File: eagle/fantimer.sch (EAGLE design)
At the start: 20 parts, among them IC1 PIC10F220, K1 PB2032-ND, Q1 2N7000-G, U1 IRM-01-5, X1 732-10957-ND

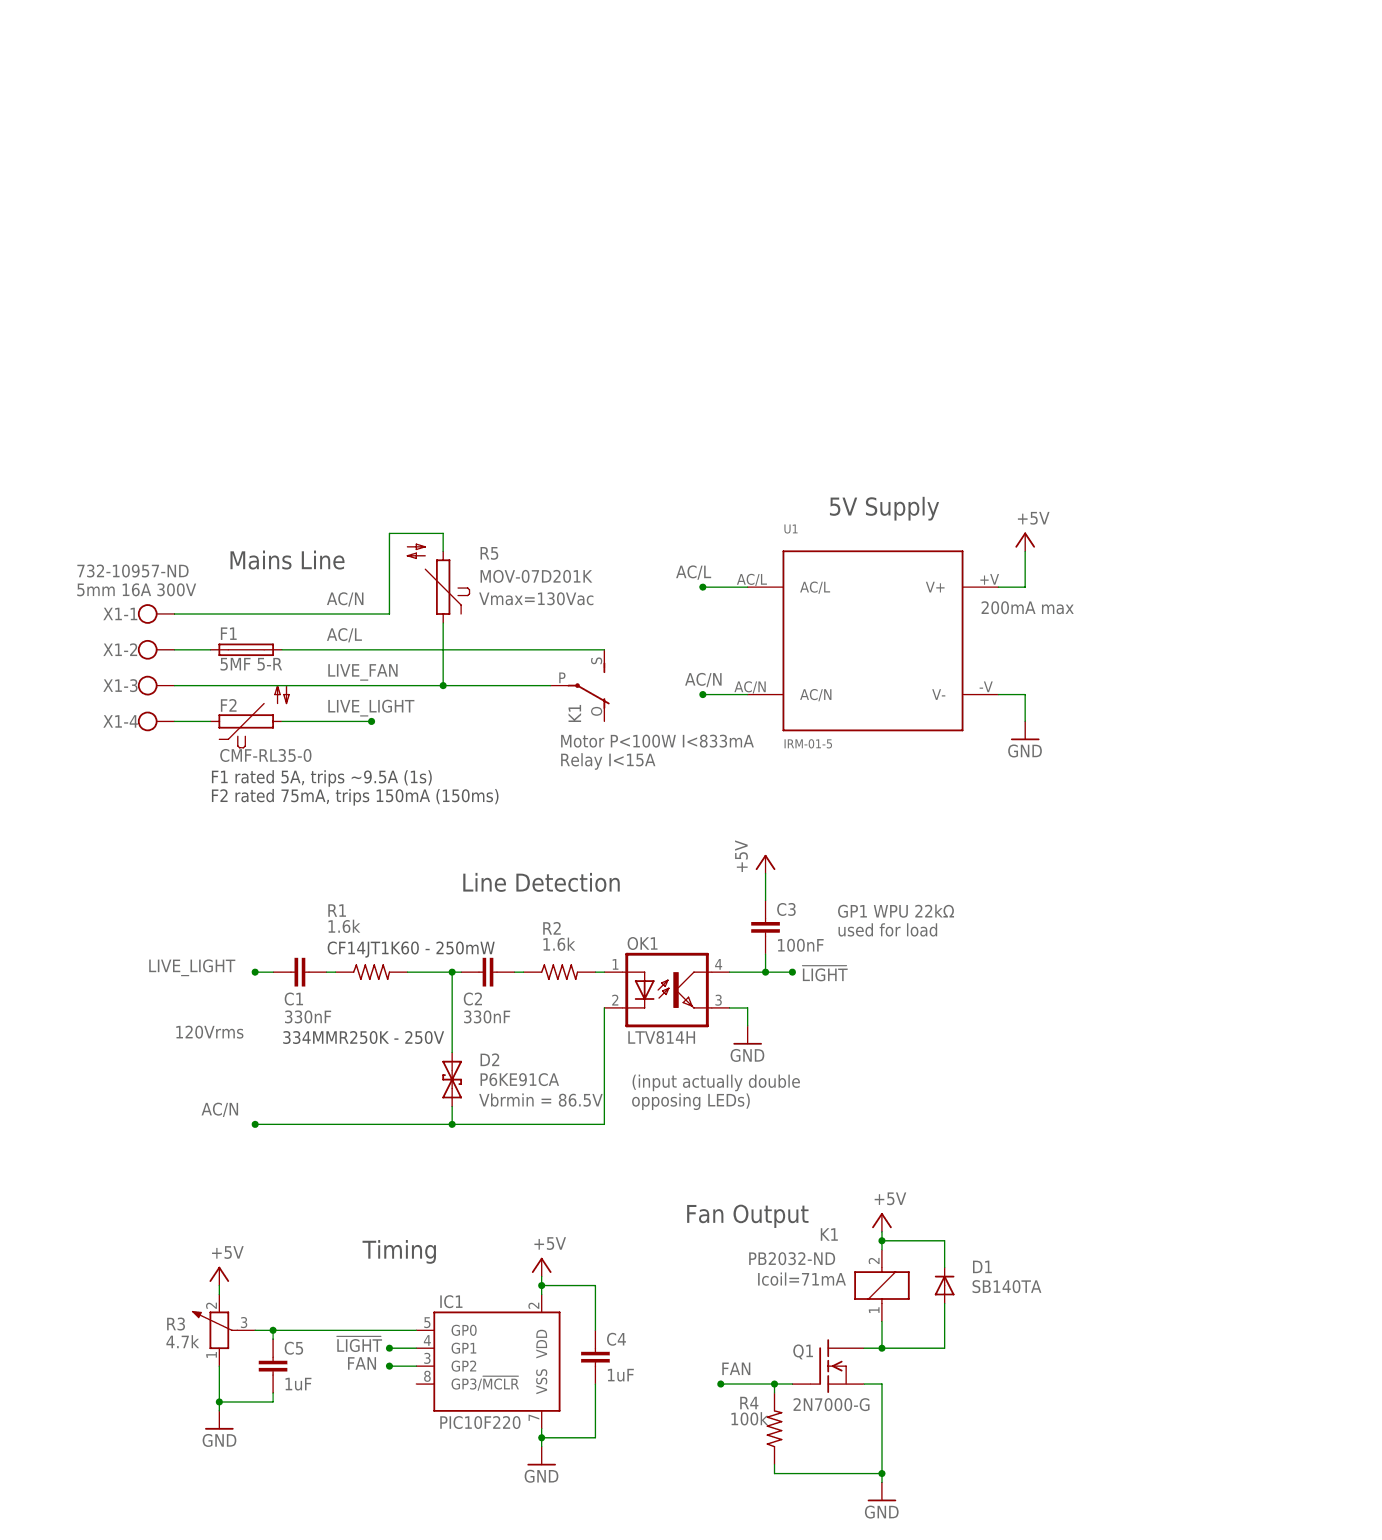
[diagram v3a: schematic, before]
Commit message: Split apart terminal pins to represent circuit logically. Swap terminal 3+4 for better routing. Drop intro text from asm. General report edits.
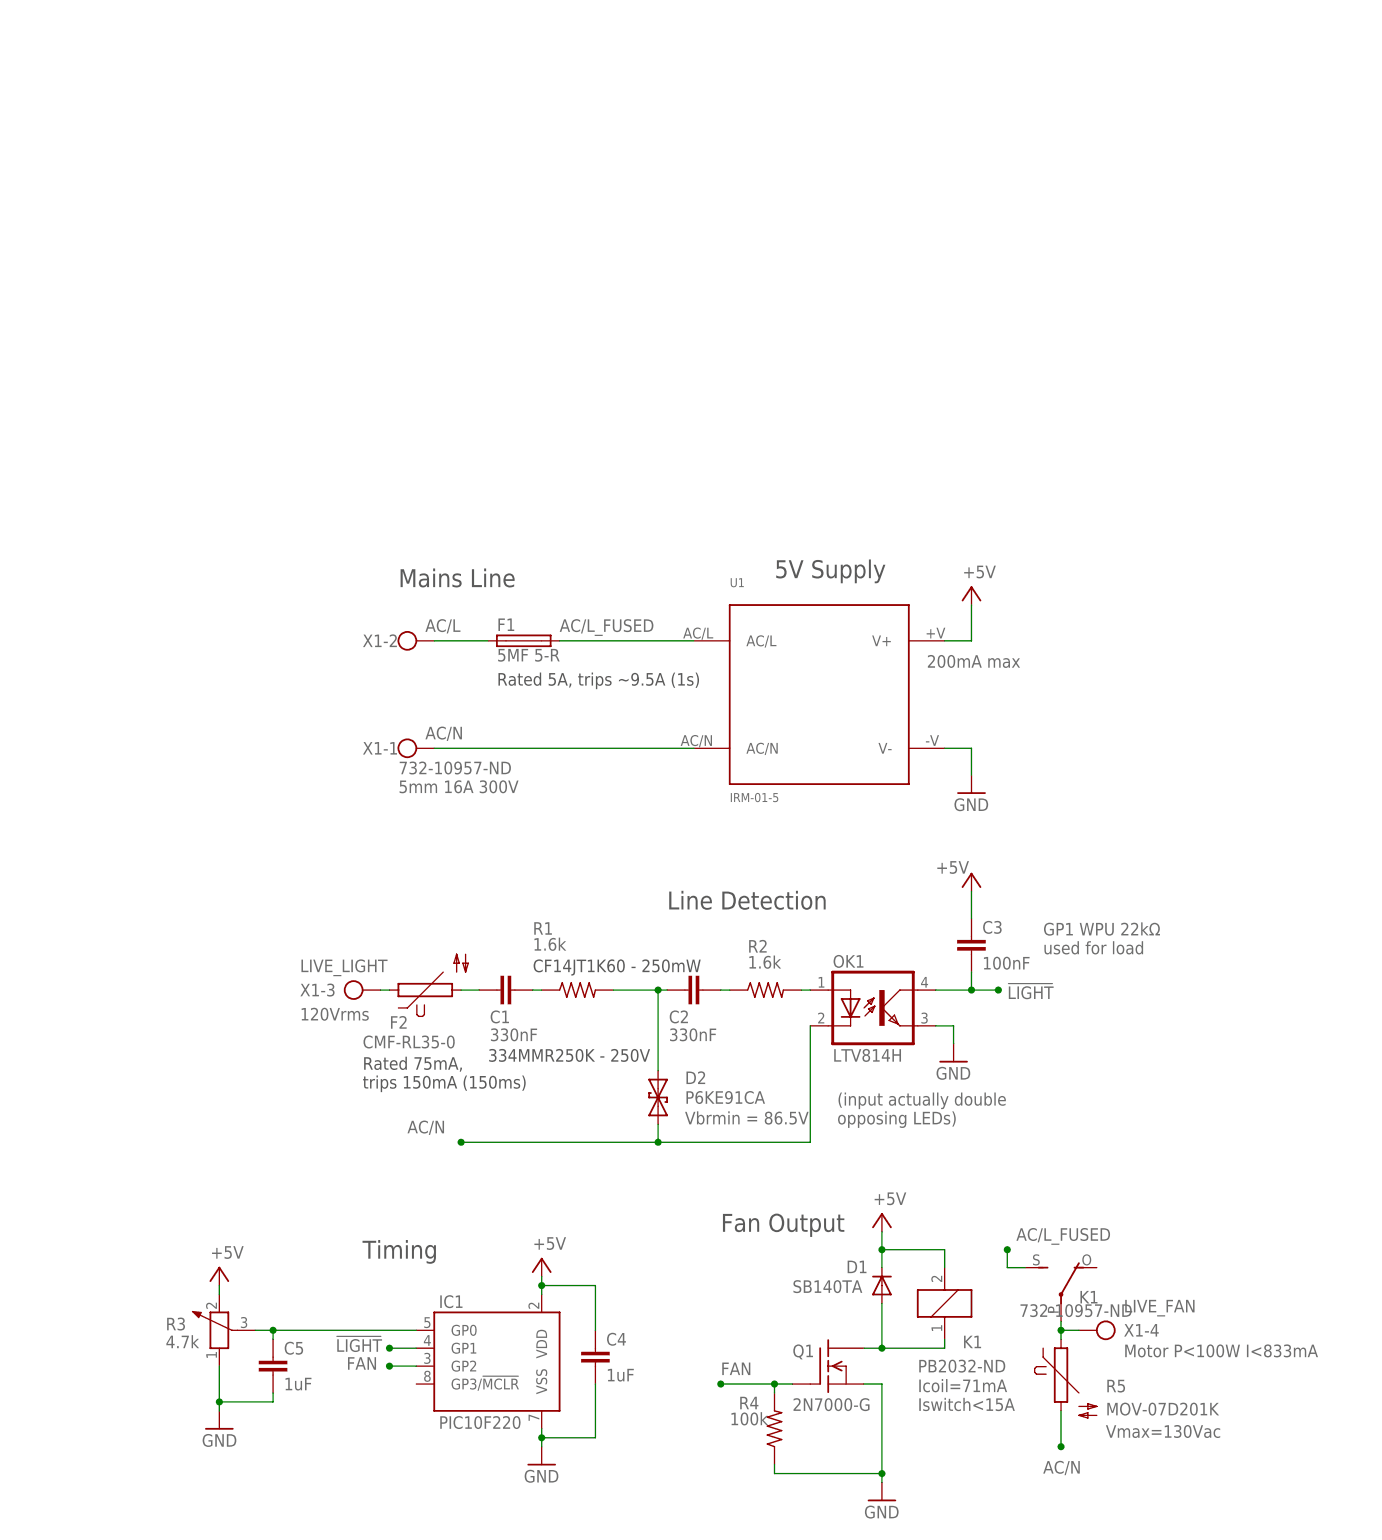
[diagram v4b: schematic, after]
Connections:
- removed net AC/L_FUSE: F1.1, X1-2.KL
- removed net LIGHT_FUSE: F2.1, X1-4.KL
- new net AC/L_FUSED: F1.2, K12.S, U1.AC/L
- new net LIVE_LIGHT_FUSED: C1.1, F2.2
- net AC/L: now also F1.1, X1-2.KL; no longer F1.2, K12.S, U1.AC/L
- net LIVE_FAN: now also X1-4.KL; no longer X1-3.KL
- net LIVE_LIGHT: now also F2.1, X1-3.KL; no longer C1.1, F2.2
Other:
- note added: "732-10957-ND 5mm 16A 300V"
- note added: "Icoil=71mA Iswitch<15A"
- note added: "Motor P<100W I<833mA"
- note added: "Rated 5A, trips ~9.5A (1s)"
- note added: "Rated 75mA, trips 150mA (150ms)"
- note removed: "5mm 16A 300V"
- note removed: "F1 rated 5A, trips ~9.5A (1s) F2 rated 75mA, trips 150mA (150ms)"
- note removed: "Icoil=71mA"
- note removed: "Motor P<100W I<833mA Relay I<15A"
- moved on the sheet: C1, C2, C3, D1, D2, F1, F2, K1, OK1, R1, R2, R5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
